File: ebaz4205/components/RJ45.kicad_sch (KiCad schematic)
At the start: 1 part

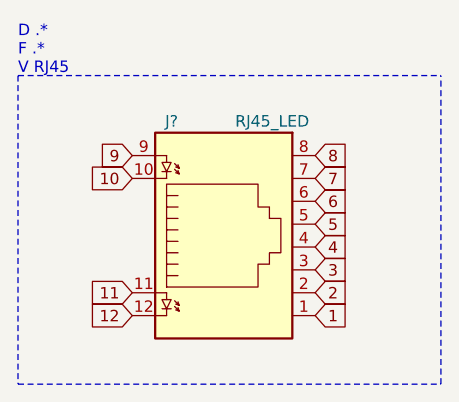
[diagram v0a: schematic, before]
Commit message: Consolidated all custom symbols into single library.
Library is available at ebaz4205/components/ebaz4205.kicad_sym

The templates and the schematics have been updated to use this library.
Keeping the original libraries for future reference.
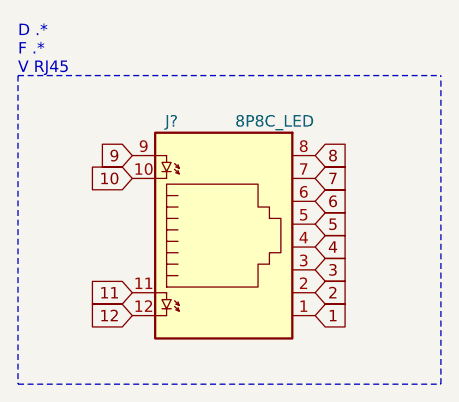
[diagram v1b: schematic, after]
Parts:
- removed J?: RJ45_LED, symbol Connector:RJ45_LED
- added J?: 8P8C_LED, symbol ebaz4205:8P8C_LED
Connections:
- net 1: now also J?.1
- net 10: now also J?.10
- net 11: now also J?.11
- net 12: now also J?.12
- net 2: now also J?.2
- net 3: now also J?.3
- net 4: now also J?.4
- net 5: now also J?.5
- net 6: now also J?.6
- net 7: now also J?.7
- net 8: now also J?.8
- net 9: now also J?.9
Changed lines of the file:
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@@
     (effects (font (size 1.27 1.27)) (justify left))
   )
-  (symbol (lib_id "Connector:RJ45_LED") (at 22.86 19.05 0) (unit 1)
+  (symbol (lib_id "ebaz4205:8P8C_LED") (at 22.86 19.05 0) (unit 1)
     (in_bom yes) (on_board yes)
     (property "Reference" "J?" (id 0) (at 17.78 5.08 0)
       (effects (font (size 1.27 1.27)) (justify right))
     )
-    (property "Value" "RJ45_LED" (id 1) (at 24.13 5.08 0)
+    (property "Value" "8P8C_LED" (id 1) (at 24.13 5.08 0)
       (effects (font (size 1.27 1.27)) (justify left))
     )
@@
   )
   (symbol_instances
-    (path "/1d2d4ac0-ae24-4298-97cf-bc2bc96f293e"
-      (reference "J?") (unit 1) (value "RJ45_LED") (footprint "")
+    (path "/b32115c4-7117-4674-9823-c792d0c2392d"
+      (reference "J?") (unit 1) (value "8P8C_LED") (footprint "")
     )
   )
